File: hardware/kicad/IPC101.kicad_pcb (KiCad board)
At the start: 2 copper layers, 100 x 140 mm, 18 parts, among them J1 IPC-100 J10, J3 IPC-100 J8A STOP, SW1 START B3F-4055, SW2 PULL B3F-4055, SW3 ADAFRUIT 504 - VERIFY PIN MAP, U1 TCA8418RTWR

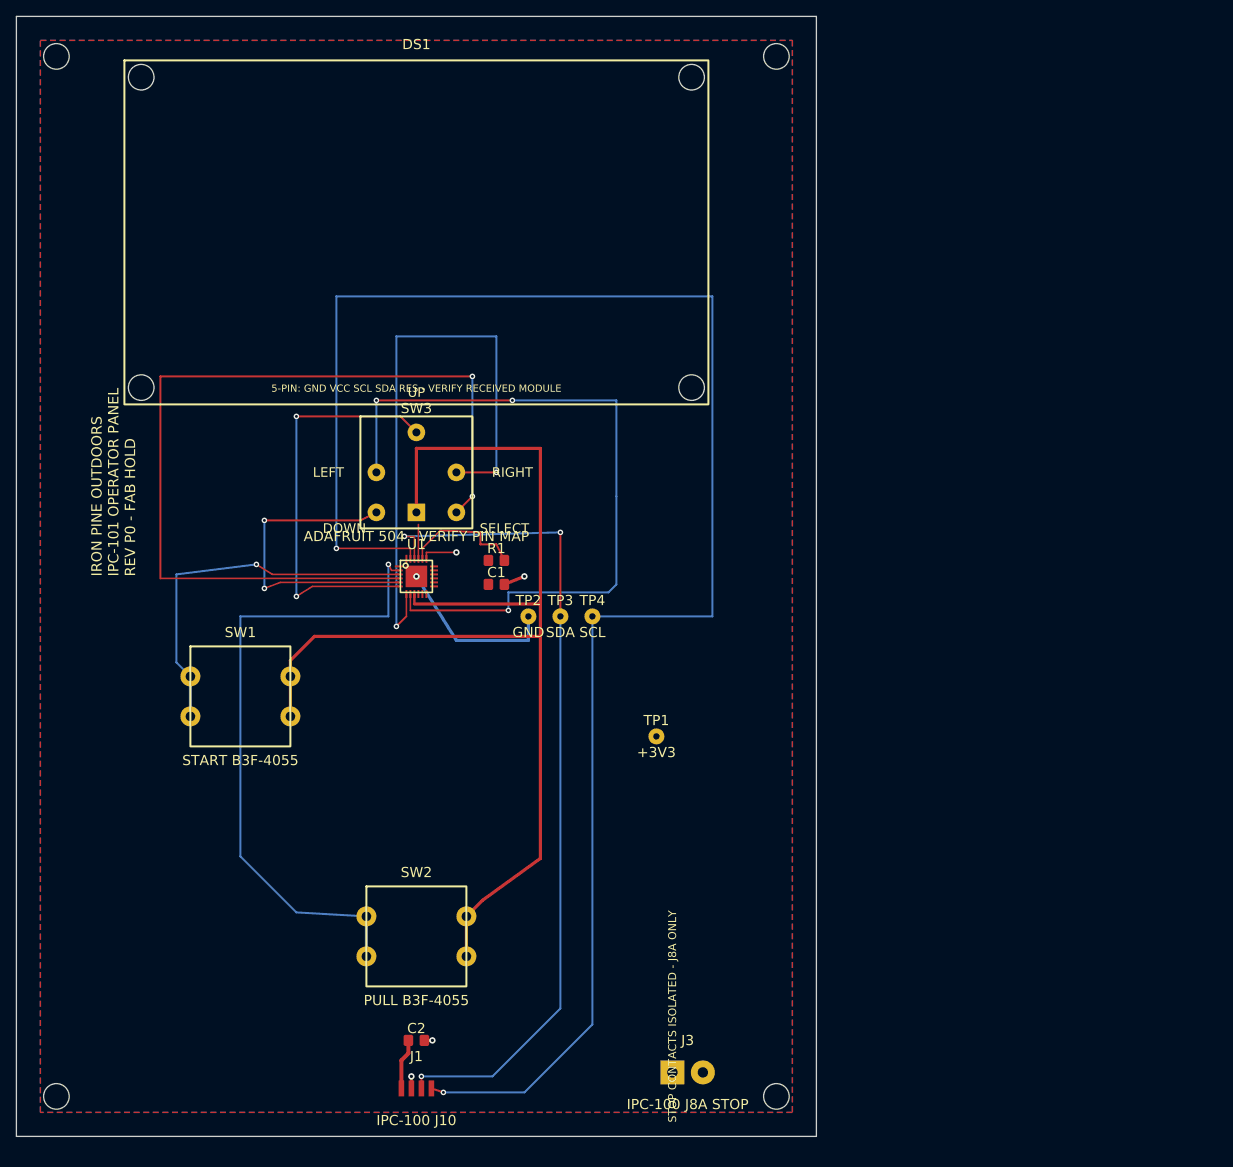
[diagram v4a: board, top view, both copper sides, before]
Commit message: Complete routed IPC-101 Rev C control board
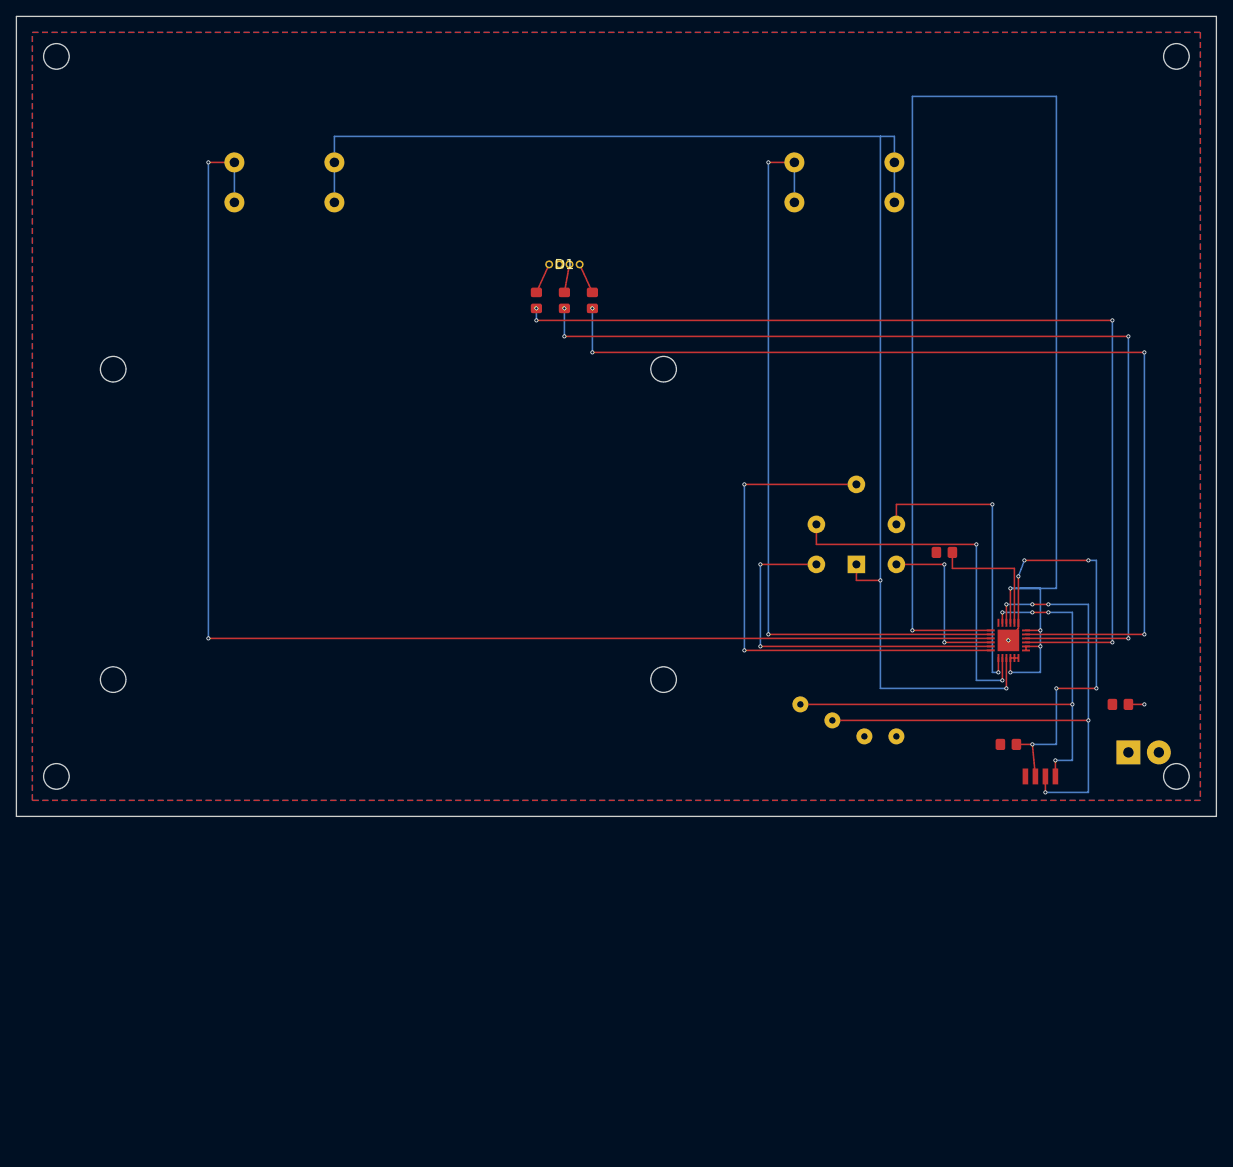
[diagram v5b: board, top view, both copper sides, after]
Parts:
- added D1: 5MM RGB COMMON ANODE, , F.Cu at (68.5, 31.0)
- added R2: 1k RED, , F.Cu at (65.0, 35.5)
- added R3: 1k GREEN, , F.Cu at (68.5, 35.5)
- added R4: 1k BLUE, , F.Cu at (72.0, 35.5)
- C1, C2: footprint IPC101:C0805 -> (none)
- DS1: footprint IPC101:HOSYOND_2.42_SSD1309_MOUNT -> (none)
- H1, H2, H3, H4: footprint MountingHole:MountingHole_3.2mm_M3 -> (none)
- J1: footprint IPC101:JST_GH_04 -> (none)
- J3: footprint IPC101:STOP_CONN -> (none)
- R1: footprint IPC101:R0805 -> (none)
- SW1: value START B3F-4055 -> ARM B3F-4055; footprint IPC101:B3F-4055 -> (none)
- SW2: footprint IPC101:B3F-4055 -> (none)
- SW3: footprint IPC101:Adafruit_504_VERIFY -> (none)
- TP1, TP2, TP3, TP4: footprint IPC101:TEST_LOOP -> (none)
- U1: footprint IPC101:TCA8418_RTW24 -> (none)
- moved SW2 108.4 mm to (103.5, 20.8)
- moved J1 87.2 mm to (128.0, 95.0)
- moved C2 82.7 mm to (124.0, 91.0)
- moved C1 79.4 mm to (138.0, 86.0)
- moved U1 74.4 mm to (124.0, 78.0)
- moved J3 69.6 mm to (139.0, 92.0)
- moved SW1 64.5 mm to (33.5, 20.8)
- moved H4 64.0 mm to (145.0, 95.0)
- moved R1 56.0 mm to (116.0, 67.0)
- moved SW3 55.4 mm to (105.0, 63.5)
- moved H2 50.0 mm to (145.0, 5.00)
- moved TP2 44.6 mm to (106.0, 90.0)
- moved H3 40.0 mm to (5.00, 95.0)
- moved DS1 36.7 mm to (46.5, 63.5)
- moved TP3 36.4 mm to (102.0, 88.0)
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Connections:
- net /R5_START renamed /R5_ARM
- U1 pad 15: /+3V3 -> /RGB_R_GPIO
- U1 pad 16: /+3V3 -> /RGB_G_GPIO
- U1 pad 17: /+3V3 -> /RGB_B_GPIO
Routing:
- net /+3V3: track 10.7 -> 191.0 mm, vias 0 -> 5
- net /SCL: track 218.8 -> 66.7 mm, vias 2 -> 5
- net /RGB_R_GPIO: track 0.00 -> 124.5 mm, vias 0 -> 4
- net /RGB_G_GPIO: track 0.00 -> 124.5 mm, vias 0 -> 4
- net /RGB_B_GPIO: track 0.00 -> 124.5 mm, vias 0 -> 4
- net /R5_ARM: track 46.7 -> 165.6 mm, vias 1 -> 2
- net /R4_SELECT: track 111.9 -> 21.5 mm
- net /R0_LEFT: track 92.5 -> 45.5 mm, vias 3 -> 2
- net /R1_RIGHT: track 75.3 -> 38.0 mm
- net /C0: track 148.0 -> 180.1 mm, vias 0 -> 2
- net /SDA: track 105.5 -> 75.4 mm, vias 3 -> 5
- net /GND: track 31.2 -> 58.6 mm, vias 5 -> 8
- net /R6_PULL: track 80.4 -> 95.0 mm, vias 1 -> 2
- net /R2_UP: track 51.5 -> 65.5 mm
- net /R3_DOWN: track 39.7 -> 46.0 mm
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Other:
- board size 100 x 140 mm -> 150 x 100 mm
- board text removed: "DOWN"
- board text removed: "IRON PINE OUTDOORS IPC-101 OPERATOR PANEL REV P0 - FAB HOLD"
- board text removed: "LEFT"
- board text removed: "RIGHT"
- board text removed: "SELECT"
- board text removed: "STOP CONTACTS ISOLATED - J8A ONLY"
- board text removed: "UP"

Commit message: Route OLED harness through IPC-101
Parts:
- added J2: OLED HARNESS OUTPUT, , F.Cu at (65.0, 70.0)
- added J4: IPC-100 J6 OLED INPUT, , F.Cu at (82.0, 95.0)
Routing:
- net /OLED_SCL: track 0.00 -> 30.7 mm, vias 0 -> 1
- net /OLED_RESET: track 0.00 -> 30.6 mm, vias 0 -> 1
- net /OLED_VCC: track 0.00 -> 27.7 mm, vias 0 -> 1
- net /OLED_GND: track 0.00 -> 27.0 mm, vias 0 -> 1
- net /OLED_SDA: track 0.00 -> 26.3 mm, vias 0 -> 1

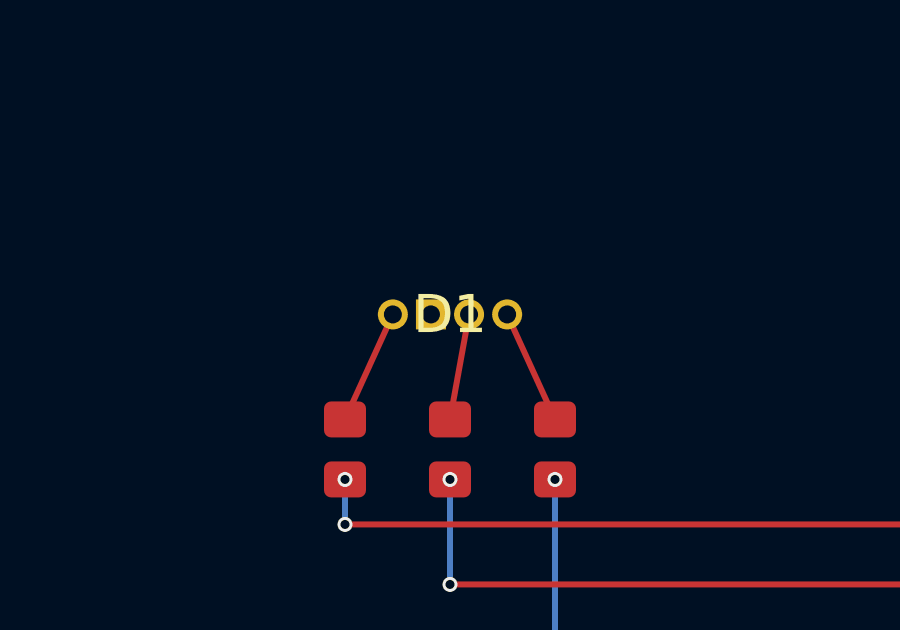
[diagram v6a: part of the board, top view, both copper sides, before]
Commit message: Restore through-hole solder mask and validate replacement fabrication package
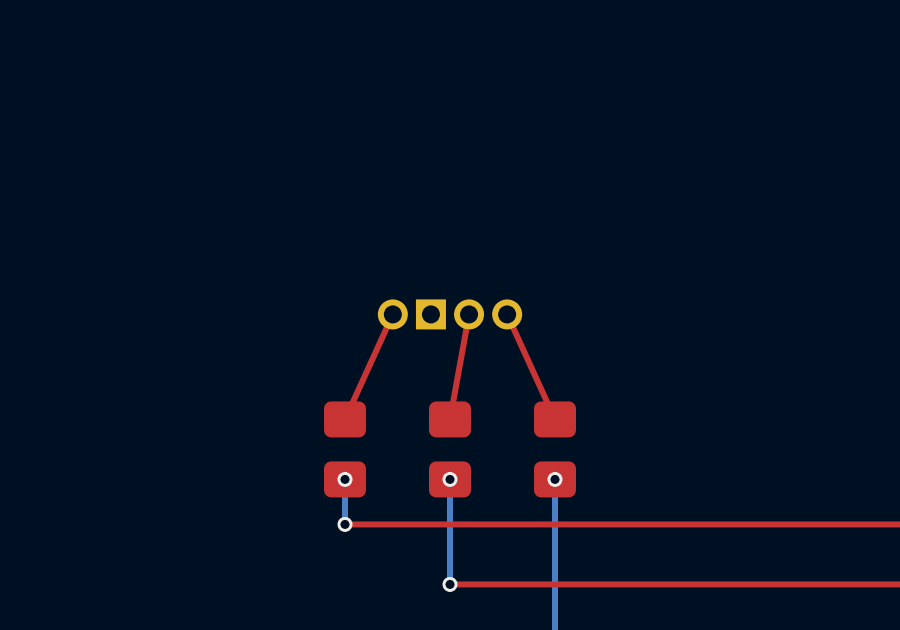
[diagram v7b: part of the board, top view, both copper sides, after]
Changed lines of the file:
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@@
 			(size 2 2)
 			(drill 0.8)
-			(layers "*.Cu")
+			(layers "*.Cu" "*.Mask")
 			(remove_unused_layers no)
 			(net "/SCL")
@@
 			(size 2 2)
 			(drill 0.8)
-			(layers "*.Cu")
+			(layers "*.Cu" "*.Mask")
 			(remove_unused_layers no)
 			(net "/GND")
@@
 		(property "Reference" "D1"
 			(at 0 0 0)
-			(layer "F.SilkS")
+			(layer "F.Fab")
 			(effects
 				(font
@@
 			(size 1 1)
 			(drill 0.6)
-			(layers "*.Cu")
+			(layers "*.Cu" "*.Mask")
 			(remove_unused_layers no)
 			(net "/RGB_R_K")
@@
 			(size 1 1)
 			(drill 0.6)
-			(layers "*.Cu")
+			(layers "*.Cu" "*.Mask")
 			(remove_unused_layers no)
 			(net "/+3V3")
@@
 			(size 1 1)
 			(drill 0.6)
-			(layers "*.Cu")
+			(layers "*.Cu" "*.Mask")
 			(remove_unused_layers no)
 			(net "/RGB_G_K")
@@
 			(size 1 1)
 			(drill 0.6)
-			(layers "*.Cu")
+			(layers "*.Cu" "*.Mask")
 			(remove_unused_layers no)
 			(net "/RGB_B_K")
@@
 			(size 3 3)
 			(drill 1.3)
-			(layers "*.Cu")
+			(layers "*.Cu" "*.Mask")
 			(remove_unused_layers no)
 			(net "/STOP_IN_RAW")
@@
 			(size 3 3)
 			(drill 1.3)
-			(layers "*.Cu")
+			(layers "*.Cu" "*.Mask")
 			(remove_unused_layers no)
 			(net "/STOP_RETURN")
@@
 			(size 2 2)
 			(drill 0.8)
-			(layers "*.Cu")
+			(layers "*.Cu" "*.Mask")
 			(remove_unused_layers no)
 			(net "/SDA")
@@
 			(size 2 2)
 			(drill 0.8)
-			(layers "*.Cu")
+			(layers "*.Cu" "*.Mask")
 			(remove_unused_layers no)
 			(net "/+3V3")
@@
 			(size 2.5 2.5)
 			(drill 1.2)
-			(layers "*.Cu")
+			(layers "*.Cu" "*.Mask")
 			(remove_unused_layers no)
 			(net "/R6_PULL")
@@
 			(size 2.5 2.5)
 			(drill 1.2)
-			(layers "*.Cu")
+			(layers "*.Cu" "*.Mask")
 			(remove_unused_layers no)
 			(net "/R6_PULL")
@@
 			(size 2.5 2.5)
 			(drill 1.2)
-			(layers "*.Cu")
+			(layers "*.Cu" "*.Mask")
 			(remove_unused_layers no)
 			(net "/C0")
@@
 			(size 2.5 2.5)
 			(drill 1.2)
-			(layers "*.Cu")
+			(layers "*.Cu" "*.Mask")
 			(remove_unused_layers no)
 			(net "/C0")
@@
 			(size 2.2 2.2)
 			(drill 1)
-			(layers "*.Cu")
+			(layers "*.Cu" "*.Mask")
 			(remove_unused_layers no)
 			(net "/C0")
@@
 			(size 2.2 2.2)
 			(drill 1)
-			(layers "*.Cu")
+			(layers "*.Cu" "*.Mask")
 			(remove_unused_layers no)
 			(net "/R0_LEFT")
@@
 			(size 2.2 2.2)
 			(drill 1)
-			(layers "*.Cu")
+			(layers "*.Cu" "*.Mask")
 			(remove_unused_layers no)
 			(net "/R1_RIGHT")
@@
 			(size 2.2 2.2)
 			(drill 1)
-			(layers "*.Cu")
+			(layers "*.Cu" "*.Mask")
 			(remove_unused_layers no)
 			(net "/R2_UP")
@@
 			(size 2.2 2.2)
 			(drill 1)
-			(layers "*.Cu")
+			(layers "*.Cu" "*.Mask")
 			(remove_unused_layers no)
 			(net "/R3_DOWN")
@@
 			(size 2.2 2.2)
 			(drill 1)
-			(layers "*.Cu")
+			(layers "*.Cu" "*.Mask")
 			(remove_unused_layers no)
 			(net "/R4_SELECT")
@@
 			(size 1.7 1.95)
 			(drill 0.95)
-			(layers "*.Cu")
+			(layers "*.Cu" "*.Mask")
 			(remove_unused_layers no)
 			(roundrect_rratio 0.147059)
@@
 			(size 1.7 1.95)
 			(drill 0.95)
-			(layers "*.Cu")
+			(layers "*.Cu" "*.Mask")
 			(remove_unused_layers no)
 			(net "/OLED_GND")
@@
 			(size 1.7 1.95)
 			(drill 0.95)
-			(layers "*.Cu")
+			(layers "*.Cu" "*.Mask")
 			(remove_unused_layers no)
 			(net "/OLED_SDA")
@@
 			(size 1.7 1.95)
 			(drill 0.95)
-			(layers "*.Cu")
+			(layers "*.Cu" "*.Mask")
 			(remove_unused_layers no)
 			(net "/OLED_SCL")
@@
 			(size 1.7 1.95)
 			(drill 0.95)
-			(layers "*.Cu")
+			(layers "*.Cu" "*.Mask")
 			(remove_unused_layers no)
 			(net "/OLED_RESET")
@@
 			(size 2.5 2.5)
 			(drill 1.2)
-			(layers "*.Cu")
+			(layers "*.Cu" "*.Mask")
 			(remove_unused_layers no)
 			(net "/R5_ARM")
@@
 			(size 2.5 2.5)
 			(drill 1.2)
-			(layers "*.Cu")
+			(layers "*.Cu" "*.Mask")
 			(remove_unused_layers no)
 			(net "/R5_ARM")
@@
 			(size 2.5 2.5)
 			(drill 1.2)
-			(layers "*.Cu")
+			(layers "*.Cu" "*.Mask")
 			(remove_unused_layers no)
 			(net "/C0")
@@
 			(size 2.5 2.5)
 			(drill 1.2)
-			(layers "*.Cu")
+			(layers "*.Cu" "*.Mask")
 			(remove_unused_layers no)
 			(net "/C0")
